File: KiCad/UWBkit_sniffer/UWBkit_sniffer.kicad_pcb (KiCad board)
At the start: 2 copper layers, 1 part, among them U1 LBUA5QJ2AB

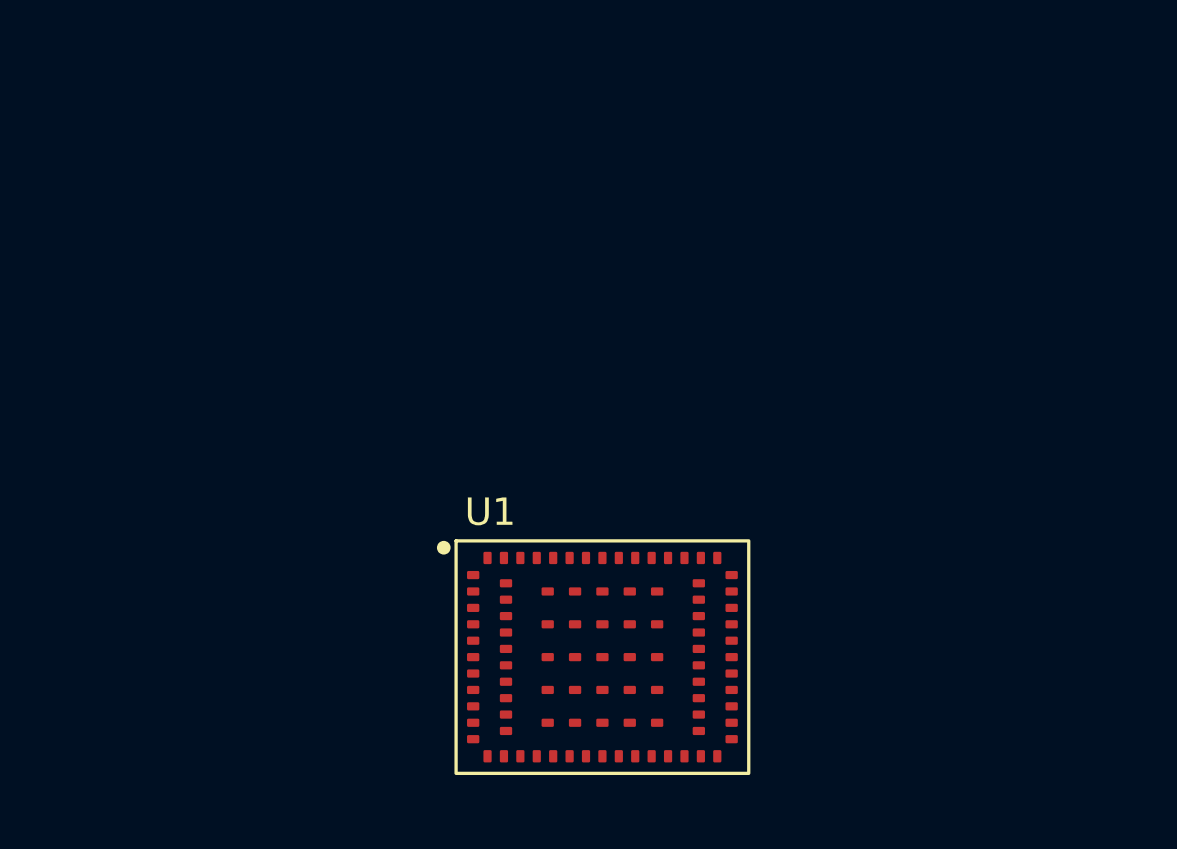
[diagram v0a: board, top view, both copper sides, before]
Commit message: Added footprint for chip antenna
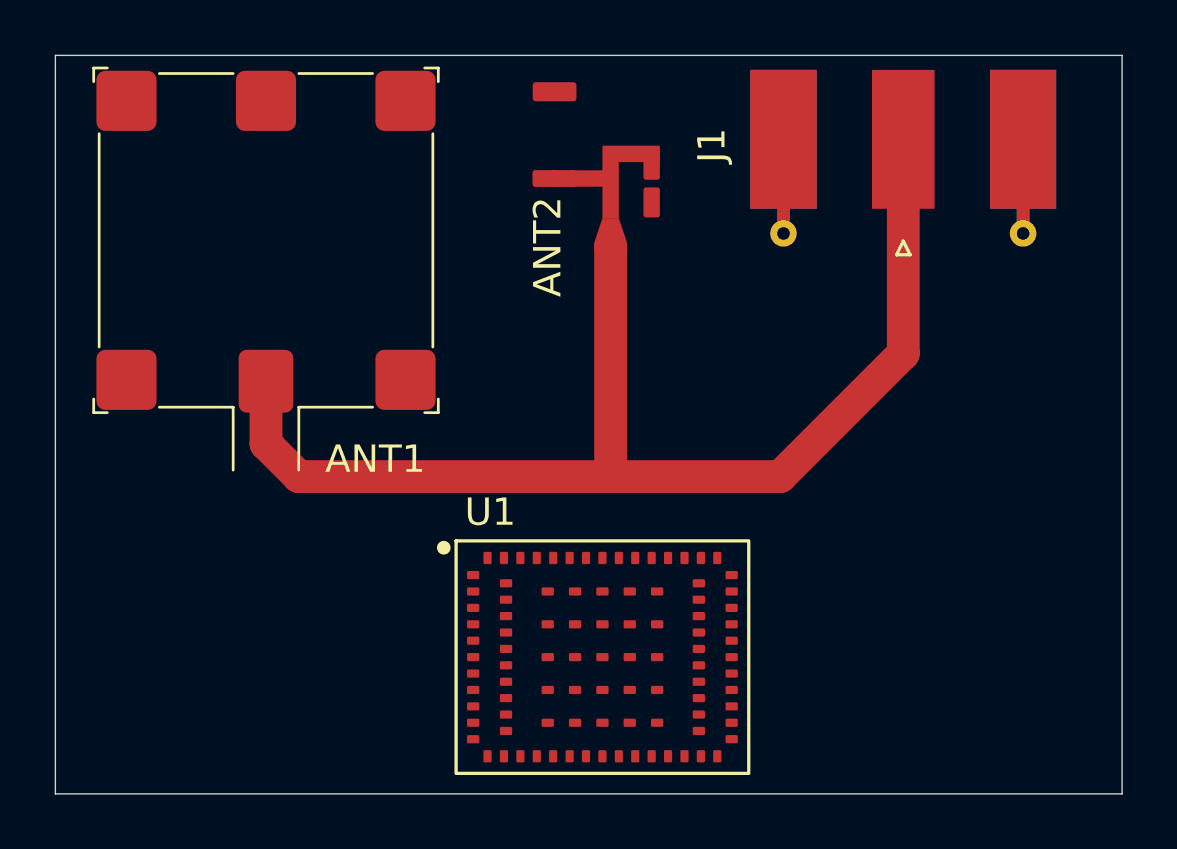
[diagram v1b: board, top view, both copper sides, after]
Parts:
- added ANT1: Taoglas_UWC.20, UWB_Antennas:Taoglas_UWC.20, F.Cu at (140.7, 68.8)
- added ANT2: Taoglas_UWA.01, UWB_Antennas:Taoglas_UWA.01, F.Cu at (152.9, 65.6)
- added J1: Conn_Coaxial, Connector_Coaxial:SMA_Molex_73251-1153_EdgeMount_Horizontal, F.Cu at (164.0, 66.8)
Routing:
- net Net-(J1-In): track 0.00 -> 44.3 mm
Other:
- board outline added: 39 x 27 mm

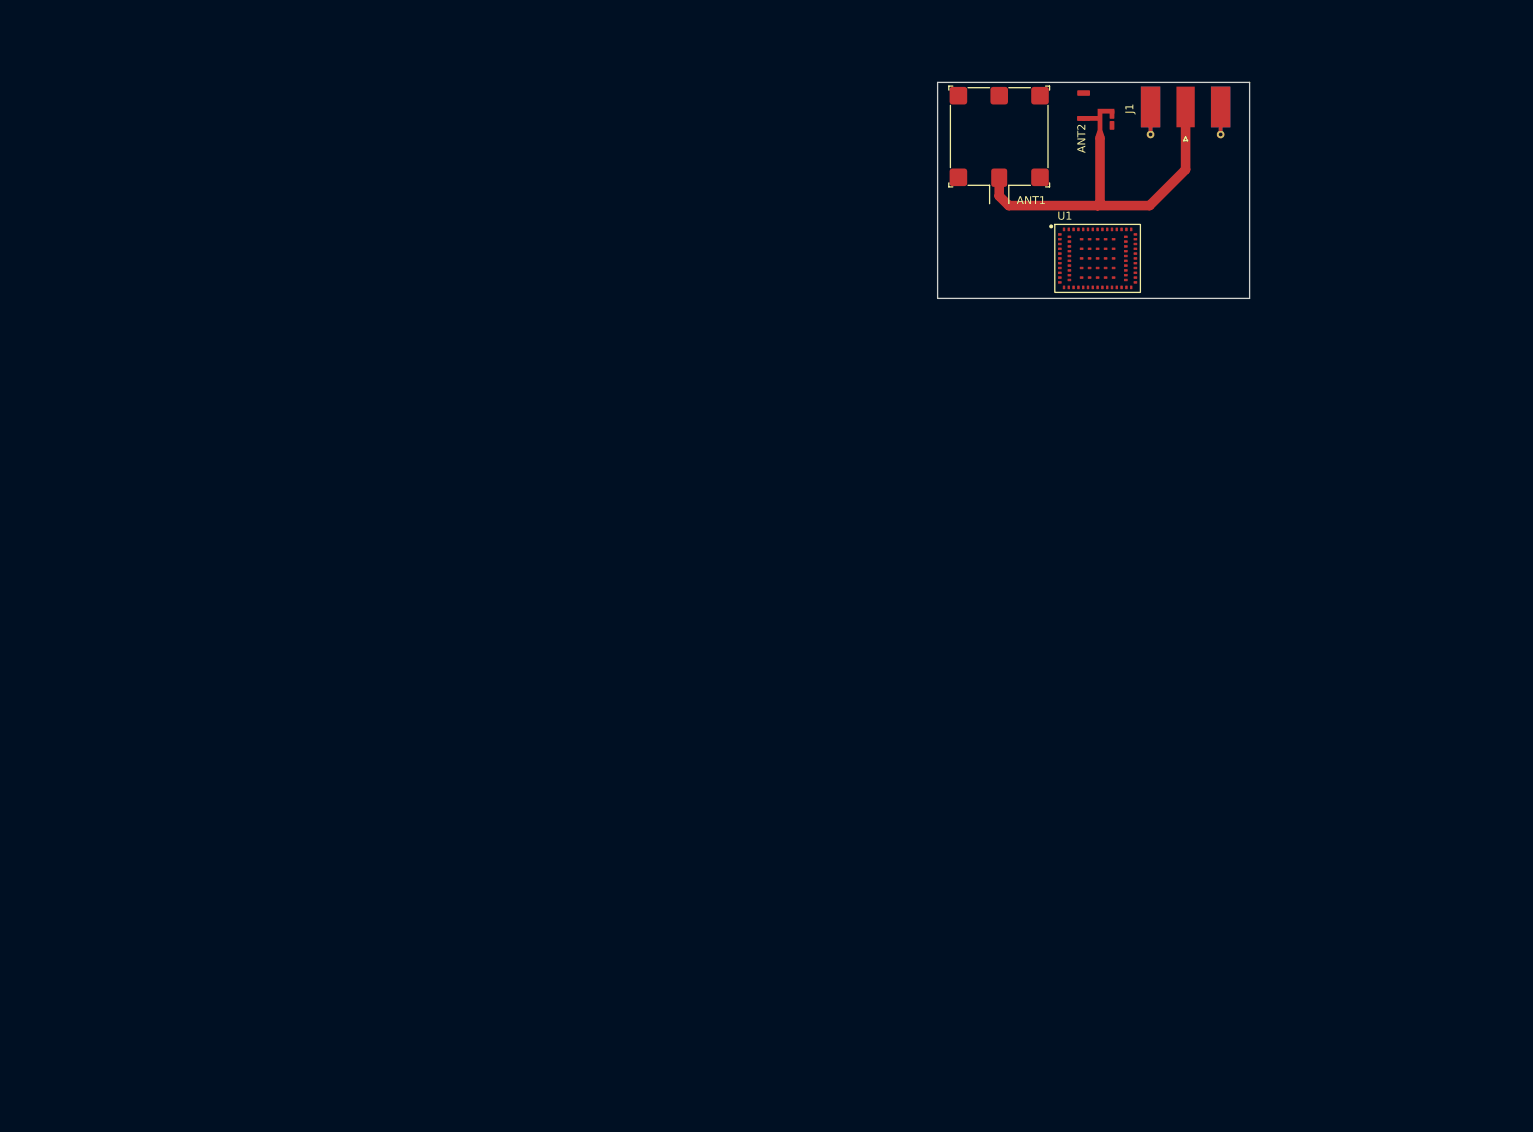
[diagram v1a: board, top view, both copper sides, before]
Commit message: Wired connections to SoC
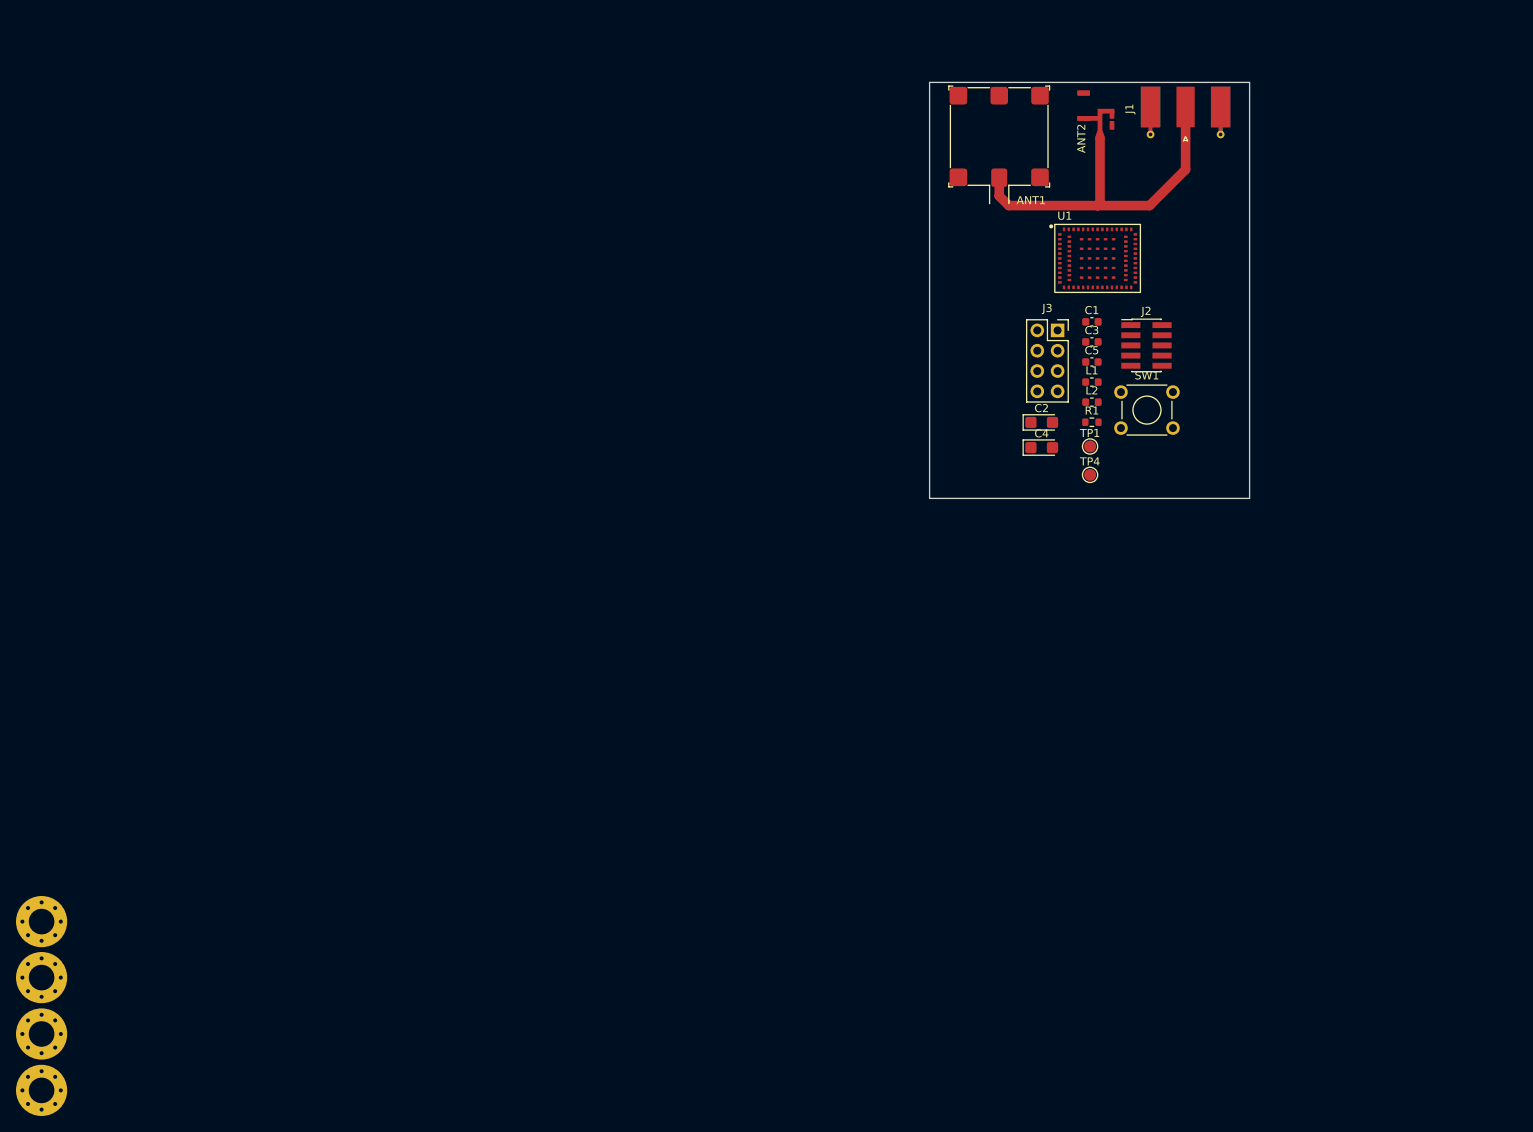
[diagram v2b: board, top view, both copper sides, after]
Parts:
- added C1: 100n, Capacitor_SMD:C_0603_1608Metric, F.Cu at (152.3, 91.9)
- added C2: 10u, Capacitor_Tantalum_SMD:CP_EIA-3216-18_Kemet-A, F.Cu at (146.0, 104.5)
- added C3: 100n, Capacitor_SMD:C_0603_1608Metric, F.Cu at (152.3, 94.4)
- added C4: 10u, Capacitor_Tantalum_SMD:CP_EIA-3216-18_Kemet-A, F.Cu at (146.0, 107.7)
- added C5: 0R, Capacitor_SMD:C_0603_1608Metric, F.Cu at (152.3, 97.0)
- added H1: MountingHole_Pad, MountingHole:MountingHole_3.2mm_M3_Pad_Via, F.Cu at (21.0, 166.9)
- added H2: MountingHole_Pad, MountingHole:MountingHole_3.2mm_M3_Pad_Via, F.Cu at (21.0, 173.9)
- added H3: MountingHole_Pad, MountingHole:MountingHole_3.2mm_M3_Pad_Via, F.Cu at (21.0, 180.9)
- added H4: MountingHole_Pad, MountingHole:MountingHole_3.2mm_M3_Pad_Via, F.Cu at (21.0, 188.0)
- added J2: Conn_SWD, Connector_PinHeader_1.27mm:PinHeader_2x05_P1.27mm_Vertical_SMD, F.Cu at (159.1, 94.9)
- added J3: Conn_GPIO, Connector_PinSocket_2.54mm:PinSocket_2x04_P2.54mm_Vertical, F.Cu at (148.0, 93.0)
- added L1: L, Inductor_SMD:L_0603_1608Metric, F.Cu at (152.3, 99.5)
- added L2: L, Inductor_SMD:L_0603_1608Metric, F.Cu at (152.3, 102.0)
- added R1: 100k, Resistor_SMD:R_0603_1608Metric, F.Cu at (152.3, 104.5)
- added SW1: SW_Push, Button_Switch_THT:SW_TH_Tactile_Omron_B3F-106x, F.Cu at (155.9, 100.7)
- added TP1: TestPoint_Small, TestPoint:TestPoint_Pad_D1.5mm, F.Cu at (152.1, 107.5)
- added TP4: TestPoint_Small, TestPoint:TestPoint_Pad_D1.5mm, F.Cu at (152.1, 111.1)
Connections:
- net Net-(J1-In) renamed /CPU/ANT1
- U1 pad 1: unconnected-(U1-GND-Pad1) -> GND
- U1 pad 16: unconnected-(U1-GND-Pad16) -> GND
- U1 pad 18: unconnected-(U1-GND-Pad18) -> GND
- U1 pad 19: unconnected-(U1-GND-Pad19) -> GND
- U1 pad 2: unconnected-(U1-P0.05/AIN3-Pad2) -> /CPU/SPIS_CLK
- U1 pad 23: unconnected-(U1-GND-Pad23) -> GND
- U1 pad 24: unconnected-(U1-SWCLK-Pad24) -> /CPU/SWCLK
- U1 pad 25: unconnected-(U1-SWDIO-Pad25) -> /CPU/SWDIO
- U1 pad 26: unconnected-(U1-GND-Pad26) -> GND
- U1 pad 28: unconnected-(U1-GND-Pad28) -> GND
- U1 pad 29: unconnected-(U1-P0.22-Pad29) -> /CPU/I2C1_SDA
- U1 pad 3: unconnected-(U1-P0.04/AIN2-Pad3) -> /CPU/SPIS_CS
- U1 pad 30: unconnected-(U1-P0.19-Pad30) -> /CPU/I2C1_SCL
- U1 pad 31: unconnected-(U1-GND-Pad31) -> GND
- U1 pad 33: unconnected-(U1-P0.24-Pad33) -> /CPU/I2C2_SDA
- U1 pad 34: unconnected-(U1-P0.21-Pad34) -> /CPU/I2C2_SCL
- U1 pad 35: unconnected-(U1-P0.18/nRESET-Pad35) -> /CPU/nRST
- U1 pad 36: unconnected-(U1-GND-Pad36) -> GND
- U1 pad 37: unconnected-(U1-ANT1-Pad37) -> Net-(U1-ANT1)
- U1 pad 38: unconnected-(U1-GND-Pad38) -> GND
- U1 pad 39: unconnected-(U1-USB_D+-Pad39) -> /CPU/USB_D+
- U1 pad 4: unconnected-(U1-P0.27-Pad4) -> /CPU/SPIS_MOSI
- U1 pad 40: unconnected-(U1-USB_D--Pad40) -> /CPU/USB_D-
- U1 pad 41: unconnected-(U1-GND-Pad41) -> GND
- U1 pad 43: unconnected-(U1-VDD2(VDDHV)-Pad43) -> +3V3
- U1 pad 44: unconnected-(U1-VDD1(VDDBAT)-Pad44) -> +3V3
- U1 pad 45: unconnected-(U1-VUSB-Pad45) -> SOC_VBUS
- U1 pad 46: unconnected-(U1-VDDMCU-Pad46) -> +3V3
- U1 pad 47: unconnected-(U1-GND-Pad47) -> GND
- U1 pad 5: unconnected-(U1-P0.26-Pad5) -> /CPU/SPIM_CLK
- U1 pad 50: unconnected-(U1-P0.08-Pad50) -> /CPU/UART_RX
- U1 pad 51: unconnected-(U1-P0.07-Pad51) -> /CPU/UART_TX
- U1 pad 52: unconnected-(U1-P0.06-Pad52) -> /CPU/SPIS_MISO
- U1 pad 53: unconnected-(U1-GND-Pad53) -> GND
- U1 pad 54: unconnected-(U1-P0.12-Pad54) -> Net-(J3-Pin_1)
- U1 pad 55: unconnected-(U1-P0.11-Pad55) -> Net-(J3-Pin_2)
- U1 pad 56: unconnected-(U1-P0.13-Pad56) -> Net-(J3-Pin_3)
- U1 pad 57: unconnected-(U1-P0.14-Pad57) -> Net-(J3-Pin_4)
- U1 pad 58: unconnected-(U1-P0.31/AIN7-Pad58) -> Net-(J3-Pin_5)
- U1 pad 59: unconnected-(U1-P0.29/AIN5-Pad59) -> Net-(J3-Pin_6)
- U1 pad 6: unconnected-(U1-P0.30/AIN6-Pad6) -> /CPU/SPIM_CS
- U1 pad 60: unconnected-(U1-P1.15-Pad60) -> Net-(J3-Pin_7)
- U1 pad 61: unconnected-(U1-P1.14-Pad61) -> Net-(J3-Pin_8)
- U1 pad 62: unconnected-(U1-GND-Pad62) -> GND
- U1 pad 7: unconnected-(U1-P0.28/AIN4-Pad7) -> /CPU/SPIM_MOSI
- U1 pad 72: unconnected-(U1-GND-Pad72) -> GND
- U1 pad 73: unconnected-(U1-GND-Pad73) -> GND
- U1 pad 74: unconnected-(U1-GND-Pad74) -> GND
- U1 pad 75: unconnected-(U1-GND-Pad75) -> GND
- U1 pad 76: unconnected-(U1-GND-Pad76) -> GND
- U1 pad 77: unconnected-(U1-GND-Pad77) -> GND
- U1 pad 78: unconnected-(U1-GND-Pad78) -> GND
- U1 pad 79: unconnected-(U1-GND-Pad79) -> GND
- U1 pad 8: unconnected-(U1-P0.02/AIN0-Pad8) -> /CPU/SPIM_MISO
- U1 pad 80: unconnected-(U1-GND-Pad80) -> GND
- U1 pad 81: unconnected-(U1-GND-Pad81) -> GND
- U1 pad 82: unconnected-(U1-GND-Pad82) -> GND
- U1 pad 83: unconnected-(U1-GND-Pad83) -> GND
- U1 pad 84: unconnected-(U1-GND-Pad84) -> GND
- U1 pad 85: unconnected-(U1-GND-Pad85) -> GND
- U1 pad 86: unconnected-(U1-GND-Pad86) -> GND
- U1 pad 87: unconnected-(U1-GND-Pad87) -> GND
- U1 pad 88: unconnected-(U1-GND-Pad88) -> GND
- U1 pad 89: unconnected-(U1-GND-Pad89) -> GND
- U1 pad 90: unconnected-(U1-GND-Pad90) -> GND
- U1 pad 91: unconnected-(U1-GND-Pad91) -> GND
- U1 pad 92: unconnected-(U1-GND-Pad92) -> GND
- U1 pad 93: unconnected-(U1-GND-Pad93) -> GND
- U1 pad 94: unconnected-(U1-GND-Pad94) -> GND
- U1 pad 95: unconnected-(U1-GND-Pad95) -> GND
- U1 pad 96: unconnected-(U1-GND-Pad96) -> GND
- U1 pad 97: unconnected-(U1-GND-Pad97) -> GND
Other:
- board size 39 x 27 mm -> 40 x 52 mm
